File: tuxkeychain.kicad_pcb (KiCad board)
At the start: 6 copper layers, 50 x 60 mm, 54 parts, among them J1 Amphenol_10104111, J3 EXPANSION, J5 Solder Pads, Q2 2N7002, SW1 B3U-1000P, U4 F1C100s, U5 TLV76701DRVx, U6 W25Q128JVS, U7 TLV76701DRVx, U8 TLV76701DRVx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

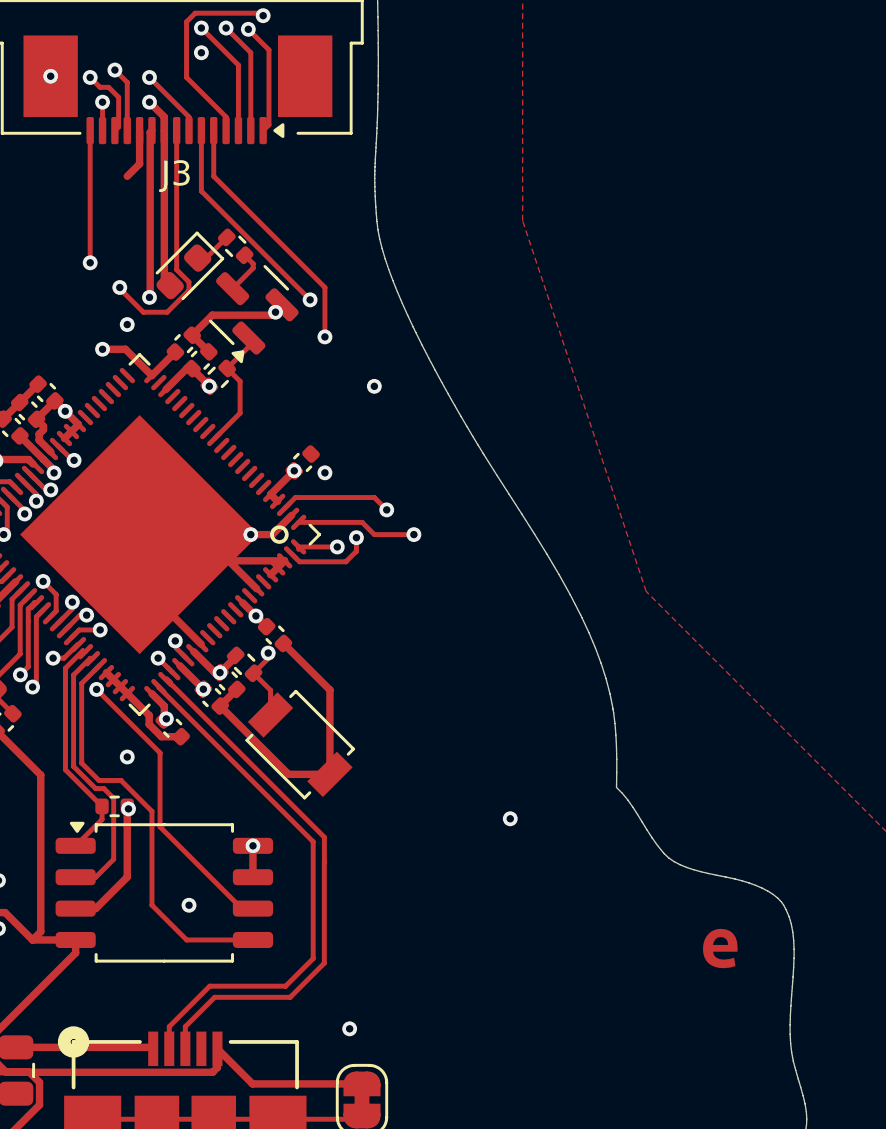
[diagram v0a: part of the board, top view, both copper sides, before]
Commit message: remove some logos and re hide references
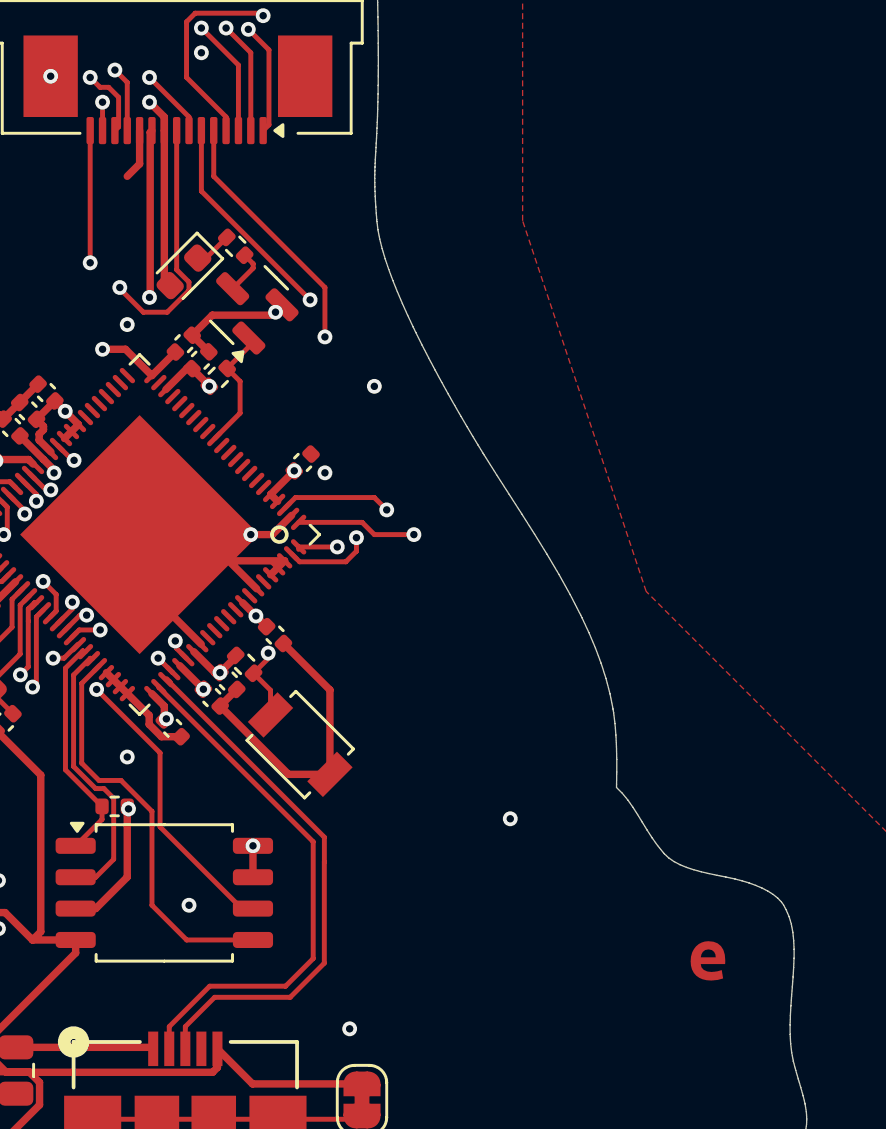
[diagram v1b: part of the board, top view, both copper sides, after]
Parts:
- removed the G*** at (129.5, 104.0)
- removed the G*** at (134.8, 103.5)
- moved G*** 7.11 mm to (133.2, 106.3)
- moved G*** 0.71 mm to (134.5, 99.0)

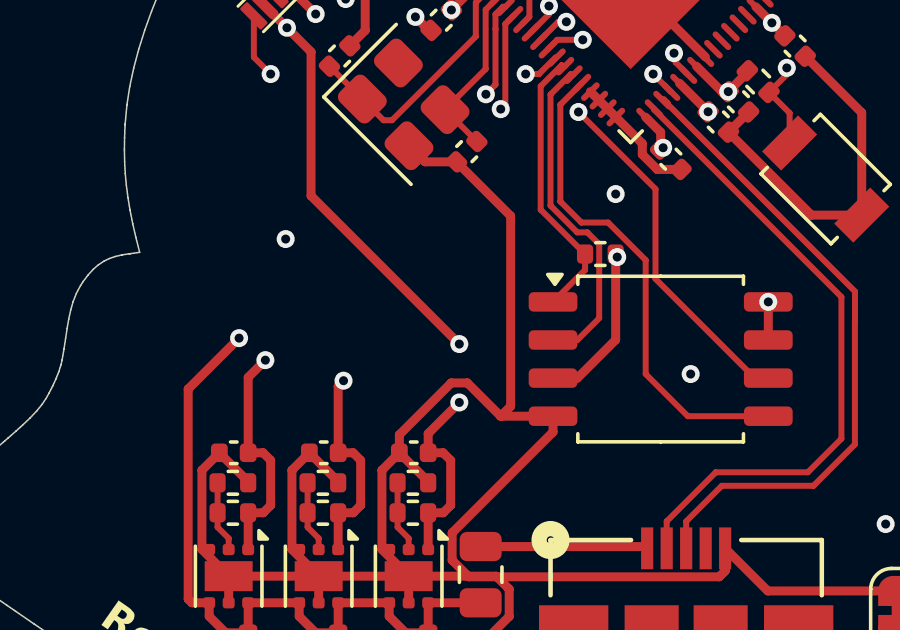
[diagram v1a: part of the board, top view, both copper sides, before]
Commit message: change led resistor and add FEL button
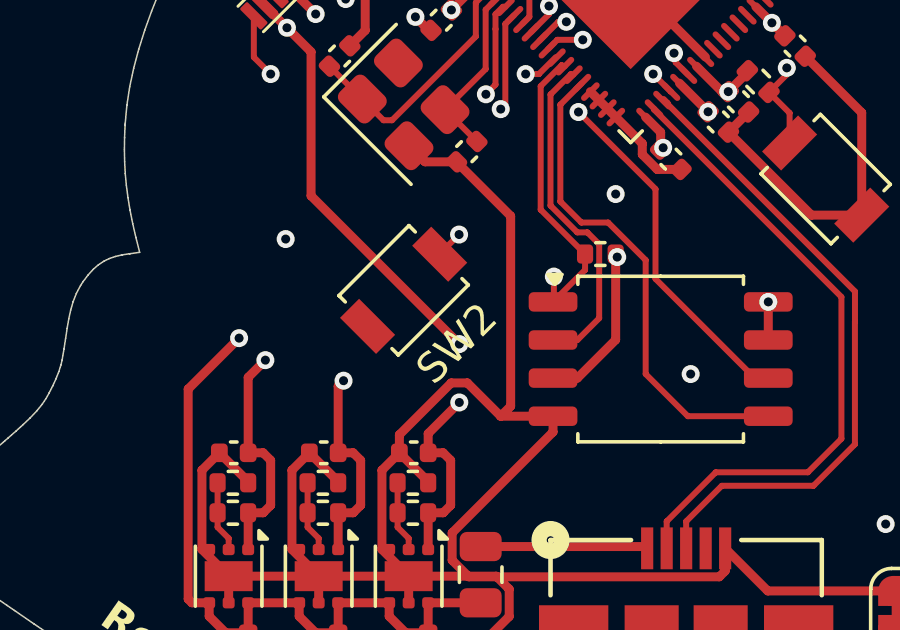
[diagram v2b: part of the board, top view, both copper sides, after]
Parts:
- removed REF**: OSHW-Symbol_6.7x6mm_Copper, Symbol:OSHW-Symbol_6.7x6mm_Copper
- added SW2: FEL, Button_Switch_SMD:SW_SPST_B3U-1000P, F.Cu at (103.9, 93.9)
- R10: value 120 -> 330
- SW1: value B3U-1000P -> RESET
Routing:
- net SPI_CS: track 9.36 -> 14.9 mm, vias 0 -> 2

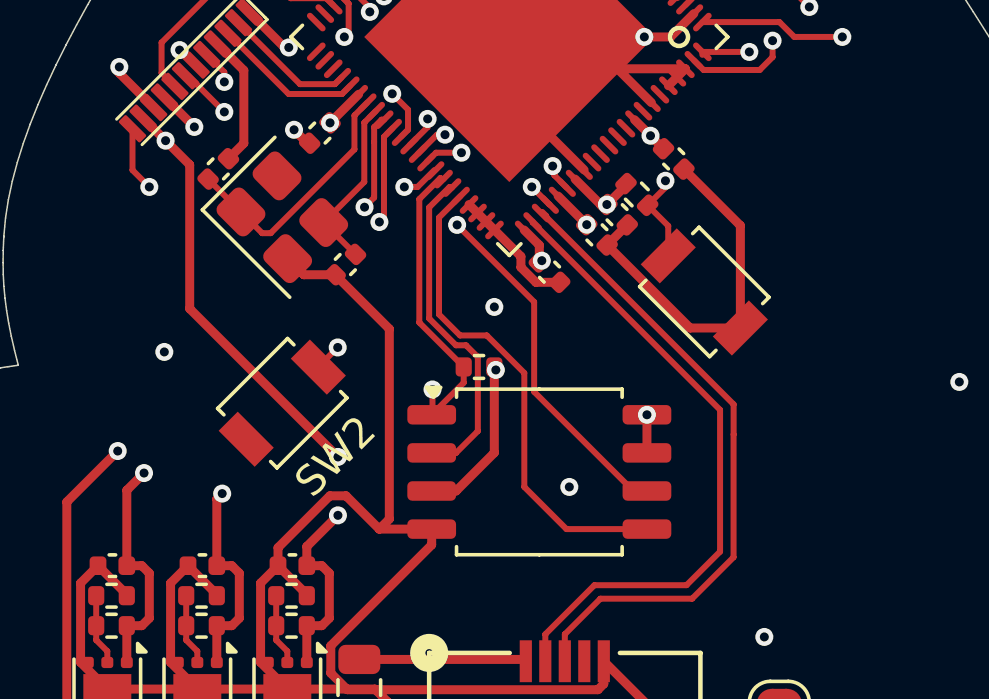
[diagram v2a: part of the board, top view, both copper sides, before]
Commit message: add labels for the rst/fel buttons
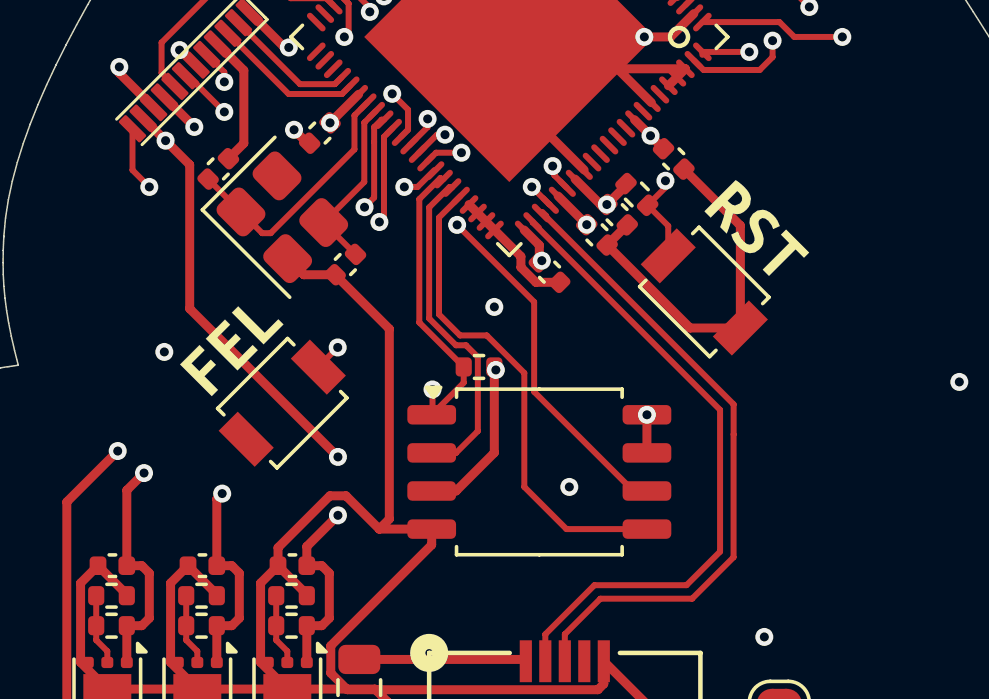
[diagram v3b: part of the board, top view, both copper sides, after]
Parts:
- added kibuzzard-687B5666: G***, kibuzzard-687B5666, F.Cu at (102.2, 92.0)
- added kibuzzard-687B569F: G***, kibuzzard-687B569F, F.Cu at (119.8, 88.2)
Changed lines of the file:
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@@
 		)
+	)
+	(footprint "kibuzzard-687B569F"
+		(layer "F.Cu")
+		(at 119.75 88.2 -45)
+		(descr "Generated with KiBuzzard")
+		(tags "kb_params=eyJBbGlnbm1lbnRDaG9pY2UiOiAiQ2VudGVyIiwgIkNhcExlZnRDaG9pY2UiOiAiIiwgIkNhcFJpZ2h0Q2hvaWNlIjogIiIsICJGb250Q29tYm9Cb3giOiAiVWJ1bnR1TW9uby1CIiwgIkhlaWdodEN0cmwiOiAxLjUsICJMYXllckNvbWJvQm94IjogIkYuU2lsa1MiLCAiTGluZVNwYWNpbmdDdHJsIjogMS41LCAiTXVsdGlMaW5lVGV4dCI6ICJSU1QiLCAiUGFkZGluZ0JvdHRvbUN0cmwiOiA1LjAsICJQYWRkaW5nTGVmdEN0cmwiOiA1LjAsICJQYWRkaW5nUmlnaHRDdHJsIjogNS4wLCAiUGFkZGluZ1RvcEN0cmwiOiA1LjAsICJXaWR0aEN0cmwiOiAxLjUsICJhZHZhbmNlZENoZWNrYm94IjogZmFsc2UsICJpbmxpbmVGb3JtYXRUZXh0Ym94IjogZmFsc2UsICJsaW5lb3ZlclN0eWxlQ2hvaWNlIjogIlNxdWFyZSIsICJsaW5lb3ZlclRoaWNrbmVzc0N0cmwiOiAxfQ==")
+		(property "Reference" "kibuzzard-687B569F"
+			(at 0 -3.830714 315)
+			(layer "F.SilkS")
+			(hide yes)
+			(effects
+				(font
+					(size 0.001 0.001)
+				)
+			)
+		)
+		(property "Value" "G***"
+			(at 0 3.830714 315)
+			(layer "F.SilkS")
+			(hide yes)
+			(effects
+				(font
+					(size 0.001 0.001)
+				)
+			)
+		)
+		(property "Datasheet" ""
+			(at 0 0 315)
+			(layer "F.Fab")
+			(hide yes)
+			(effects
+				(font
+					(size 1.27 1.27)
+					(thickness 0.15)
+				)
+			)
+		)
+		(property "Description" ""
+			(at 0 0 315)
+			(layer "F.Fab")
+			(hide yes)
+			(effects
+				(font
+					(size 1.27 1.27)
+					(thickness 0.15)
+				)
+			)
+		)
+		(attr board_only exclude_from_pos_files exclude_from_bom)
+		(fp_poly
+			(pts
+				(xy 1.721729 -0.748788) (xy 1.721729 -0.501616) (xy 1.326737 -0.501616) (xy 1.326737 0.751212) (xy 1.026252 0.751212)
+				(xy 1.026252 -0.501616) (xy 0.63126 -0.501616) (xy 0.63126 -0.748788) (xy 1.721729 -0.748788)
+			)
+			(stroke
+				(width 0)
+				(type solid)
+			)
+			(fill yes)
+			(layer "F.SilkS")
+		)
+		(fp_poly
+			(pts
+				(xy -1.334006 -0.765751) (xy -1.211632 -0.758481) (xy -1.101373 -0.736672) (xy -1.004443 -0.699717)
+				(xy -0.922052 -0.647011) (xy -0.806947 -0.493134) (xy -0.776959 -0.391659) (xy -0.766963 -0.273829)
+				(xy -0.780291 -0.149031) (xy -0.820275 -0.03635) (xy -0.891155 0.057553) (xy -0.997173 0.12601)
+				(xy -0.909935 0.265347) (xy -0.820276 0.425283) (xy -0.736672 0.592488) (xy -0.667609 0.751212)
+				(xy -0.98021 0.751212) (xy -1.040489 0.608542) (xy -1.109855 0.471325) (xy -1.18649 0.335925) (xy -1.268578 0.198708)
+				(xy -1.423667 0.198708) (xy -1.423668 -0.048465) (xy -1.358239 -0.048465) (xy -1.226777 -0.063308)
+				(xy -1.137722 -0.107835) (xy -1.069871 -0.276252) (xy -1.088045 -0.379241) (xy -1.142569 -0.450727)
+				(xy -1.226777 -0.492528) (xy -1.334006 -0.506462) (xy -1.375202 -0.50525) (xy -1.423668 -0.499192)
+				(xy -1.423668 -0.048465) (xy -1.423667 0.198708) (xy -1.423667 0.751213) (xy -1.721729 0.751212)
+				(xy -1.721729 -0.726979) (xy -1.62601 -0.745153) (xy -1.520598 -0.75727) (xy -1.418821 -0.763327)
+				(xy -1.334006 -0.765751)
+			)
+			(stroke
+				(width 0)
+				(type solid)
+			)
+			(fill yes)
+			(layer "F.SilkS")
+		)
+		(fp_poly
+			(pts
+				(xy -0.078756 0.533118) (xy 0.046042 0.517367) (xy 0.124798 0.473748) (xy 0.164782 0.410743) (xy 0.175687 0.339256)
+				(xy 0.149031 0.256866) (xy 0.081179 0.192649) (xy -0.010905 0.141761) (xy -0.112682 0.099354) (xy -0.253231 0.043619)
+				(xy -0.385299 -0.036349) (xy -0.483441 -0.1563) (xy -0.522213 -0.33441) (xy -0.487985 -0.522213)
+				(xy -0.385299 -0.663974) (xy -0.282579 -0.729941) (xy -0.156974 -0.769521) (xy -0.008481 -0.782713)
+				(xy 0.12086 -0.774838) (xy 0.232632 -0.751212) (xy 0.405897 -0.680937) (xy 0.318659 -0.450727) (xy 0.184167 -0.508885)
+				(xy 0.013328 -0.533118) (xy -0.118605 -0.514001) (xy -0.197765 -0.456651) (xy -0.224152 -0.361066)
+				(xy -0.199919 -0.284734) (xy -0.138126 -0.226575) (xy -0.053312 -0.181745) (xy 0.039983 -0.145396)
+				(xy 0.186591 -0.086026) (xy 0.327142 0.001212) (xy 0.432553 0.136914) (xy 0.463449 0.228695) (xy 0.473748 0.34168)
+				(xy 0.439519 0.528574) (xy 0.336834 0.667609) (xy 0.229806 0.731556) (xy 0.091276 0.769925) (xy -0.078756 0.782713)
+				(xy -0.246567 0.772718) (xy -0.376816 0.74273) (xy -0.544023 0.668821) (xy -0.456785 0.426494) (xy -0.300485 0.499192)
+				(xy -0.199616 0.524637) (xy -0.078756 0.533118)
+			)
+			(stroke
+				(width 0)
+				(type solid)
+			)
+			(fill yes)
+			(layer "F.SilkS")
+		)
+		(embedded_fonts no)
 	)
 	(footprint "Capacitor_SMD:C_0402_1005Metric"
@@
 			(at 0 -2.5 45)
 			(layer "F.SilkS")
+			(hide yes)
 			(effects
 				(font
@@
 		)
 	)
+	(footprint "kibuzzard-687B5666"
+		(layer "F.Cu")
+		(at 102.25 91.95 45)
+		(descr "Generated with KiBuzzard")
+		(tags "kb_params=eyJBbGlnbm1lbnRDaG9pY2UiOiAiQ2VudGVyIiwgIkNhcExlZnRDaG9pY2UiOiAiIiwgIkNhcFJpZ2h0Q2hvaWNlIjogIiIsICJGb250Q29tYm9Cb3giOiAiVWJ1bnR1TW9uby1CIiwgIkhlaWdodEN0cmwiOiAxLjUsICJMYXllckNvbWJvQm94IjogIkYuU2lsa1MiLCAiTGluZVNwYWNpbmdDdHJsIjogMS41LCAiTXVsdGlMaW5lVGV4dCI6ICJGRUwiLCAiUGFkZGluZ0JvdHRvbUN0cmwiOiA1LjAsICJQYWRkaW5nTGVmdEN0cmwiOiA1LjAsICJQYWRkaW5nUmlnaHRDdHJsIjogNS4wLCAiUGFkZGluZ1RvcEN0cmwiOiA1LjAsICJXaWR0aEN0cmwiOiAxLjUsICJhZHZhbmNlZENoZWNrYm94IjogZmFsc2UsICJpbmxpbmVGb3JtYXRUZXh0Ym94IjogZmFsc2UsICJsaW5lb3ZlclN0eWxlQ2hvaWNlIjogIlNxdWFyZSIsICJsaW5lb3ZlclRoaWNrbmVzc0N0cmwiOiAxfQ==")
+		(property "Reference" "kibuzzard-687B5666"
+			(at 0 -3.798001 45)
+			(layer "F.SilkS")
+			(hide yes)
+			(effects
+				(font
+					(size 0.001 0.001)
+				)
+			)
+		)
+		(property "Value" "G***"
+			(at 0 3.798001 45)
+			(layer "F.SilkS")
+			(hide yes)
+			(effects
+				(font
+					(size 0.001 0.001)
+				)
+			)
+		)
+		(property "Datasheet" ""
+			(at 0 0 45)
+			(layer "F.Fab")
+			(hide yes)
+			(effects
+				(font
+					(size 1.27 1.27)
+					(thickness 0.15)
+				)
+			)
+		)
+		(property "Description" ""
+			(at 0 0 45)
+			(layer "F.Fab")
+			(hide yes)
+			(effects
+				(font
+					(size 1.27 1.27)
+					(thickness 0.15)
+				)
+			)
+		)
+		(attr board_only exclude_from_pos_files exclude_from_bom)
+		(fp_poly
+			(pts
+				(xy 1.69265 0.75) (xy 0.75 0.75) (xy 0.75 -0.75) (xy 1.050485 -0.75) (xy 1.050485 0.502826) (xy 1.692649 0.502827)
+				(xy 1.69265 0.75)
+			)
+			(stroke
+				(width 0)
+				(type solid)
+			)
+			(fill yes)
+			(layer "F.SilkS")
+		)
+		(fp_poly
+			(pts
+				(xy -1.69265 0.75) (xy -1.69265 -0.75) (xy -0.774232 -0.75) (xy -0.774233 -0.502827) (xy -1.394588 -0.502827)
+				(xy -1.394588 -0.139338) (xy -0.851777 -0.139338) (xy -0.851777 0.107835) (xy -1.394588 0.107834)
+				(xy -1.394589 0.75) (xy -1.69265 0.75)
+			)
+			(stroke
+				(width 0)
+				(type solid)
+			)
+			(fill yes)
+			(layer "F.SilkS")
+		)
+		(fp_poly
+			(pts
+				(xy -0.481018 0.75) (xy -0.481018 -0.75) (xy 0.427706 -0.75) (xy 0.427706 -0.502827) (xy -0.182956 -0.502827)
+				(xy -0.182956 -0.165994) (xy 0.347737 -0.165994) (xy 0.347738 0.081179) (xy -0.182956 0.081179)
+				(xy -0.182956 0.502827) (xy 0.481018 0.502826) (xy 0.481018 0.75) (xy -0.481018 0.75)
+			)
+			(stroke
+				(width 0)
+				(type solid)
+			)
+			(fill yes)
+			(layer "F.SilkS")
+		)
+		(embedded_fonts no)
+	)
 	(footprint "Capacitor_SMD:C_0402_1005Metric"

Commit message: change armv8 logo
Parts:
- moved G*** 4.60 mm to (128.8, 100.5)

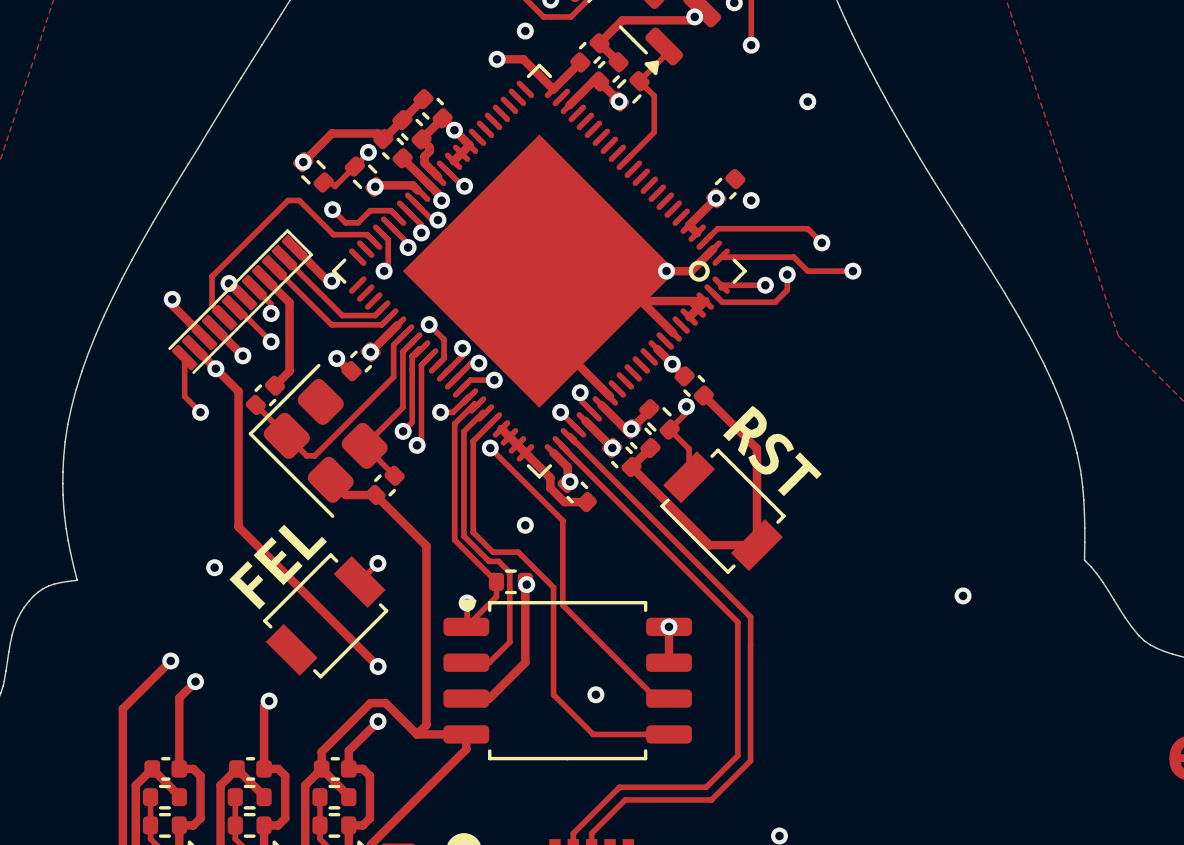
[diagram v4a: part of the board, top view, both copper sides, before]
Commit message: add uart header
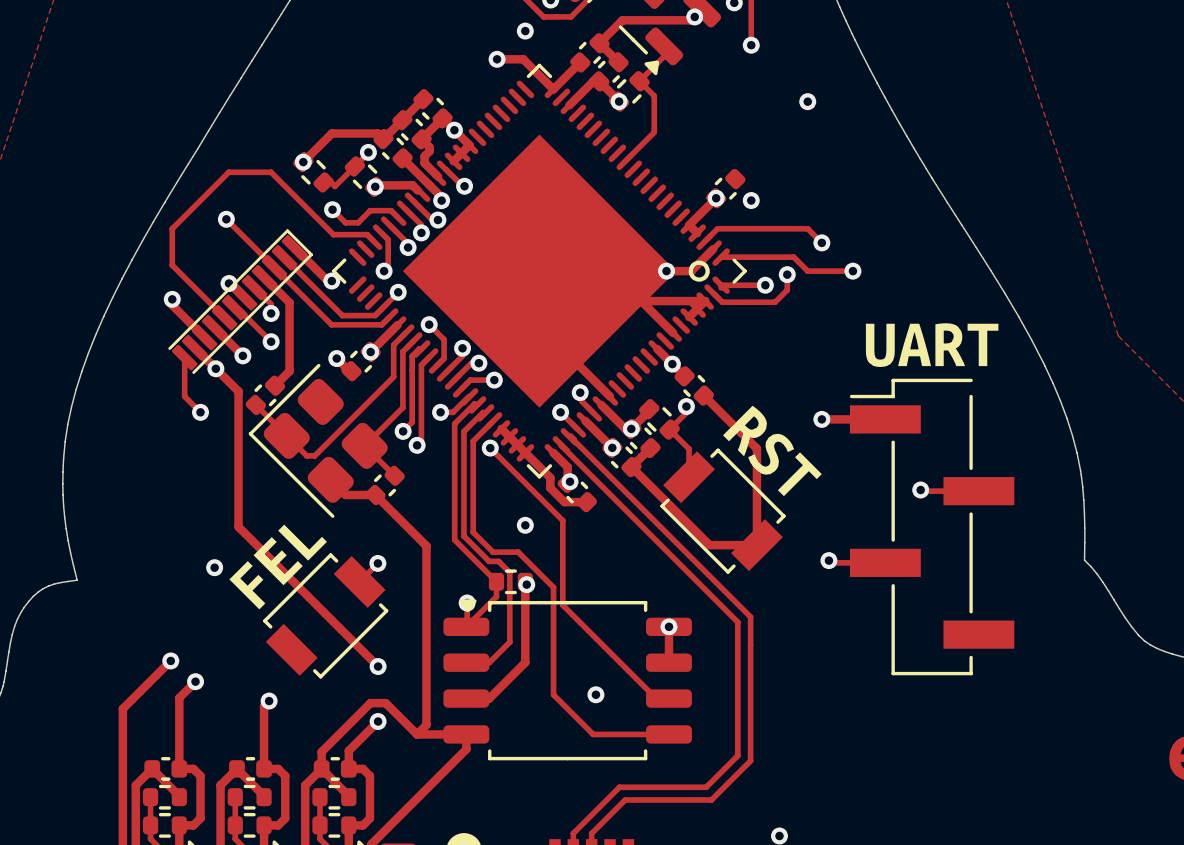
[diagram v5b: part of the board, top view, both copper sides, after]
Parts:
- added J2: UART, Connector_PinHeader_2.54mm:PinHeader_1x04_P2.54mm_Vertical_SMD_Pin1Left, F.Cu at (125.4, 90.8)
- added kibuzzard-688DDBDB: G***, kibuzzard-688DDBDB, F.Cu at (125.4, 84.3)
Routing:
- net UART_RX: track 5.03 -> 37.2 mm, vias 0 -> 2
- net UART_TX: track 4.38 -> 29.0 mm, vias 0 -> 2
- net +5V: track 65.3 -> 87.1 mm, vias 3 -> 4
- net SPI1_CS: track 9.07 -> 12.9 mm
- net GND: vias 14 -> 13
